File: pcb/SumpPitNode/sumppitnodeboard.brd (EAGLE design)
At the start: 100 x 80 mm, 36 parts, among them IC1 7805T

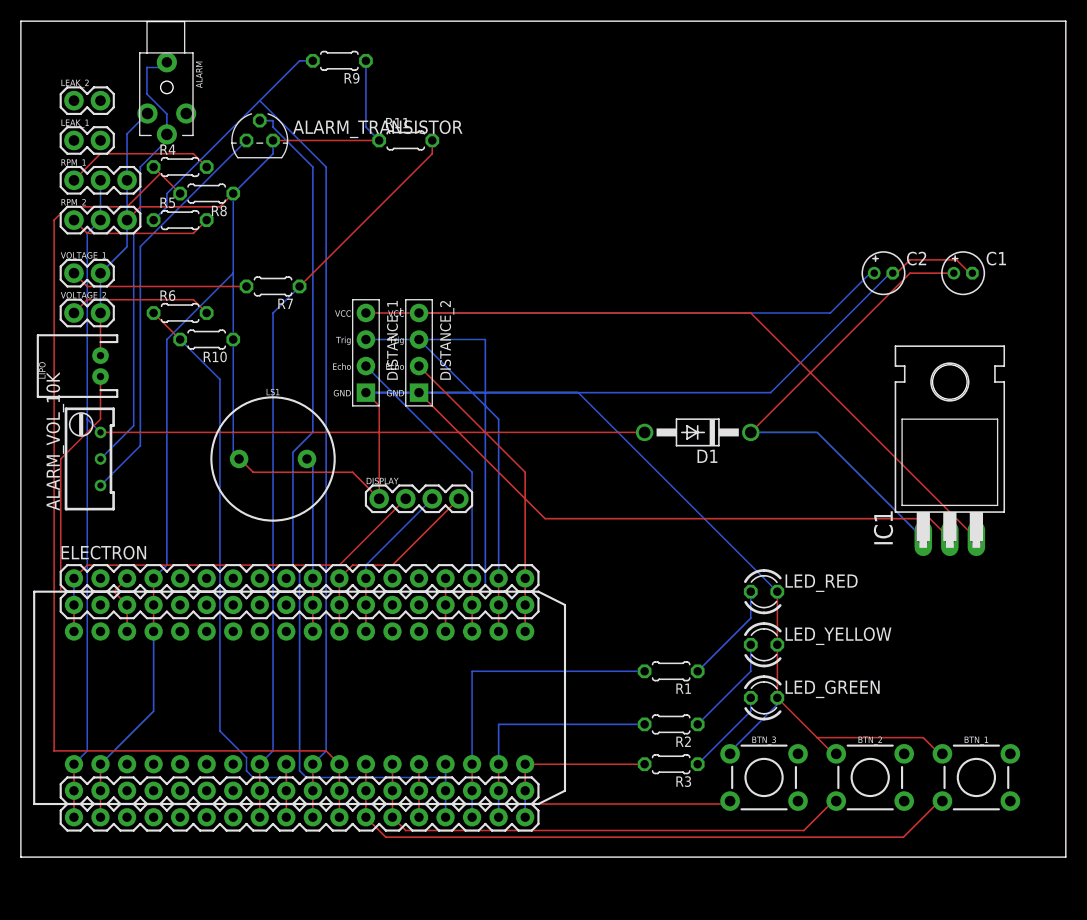
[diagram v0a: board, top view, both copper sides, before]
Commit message: Generate board, connect more sensors.
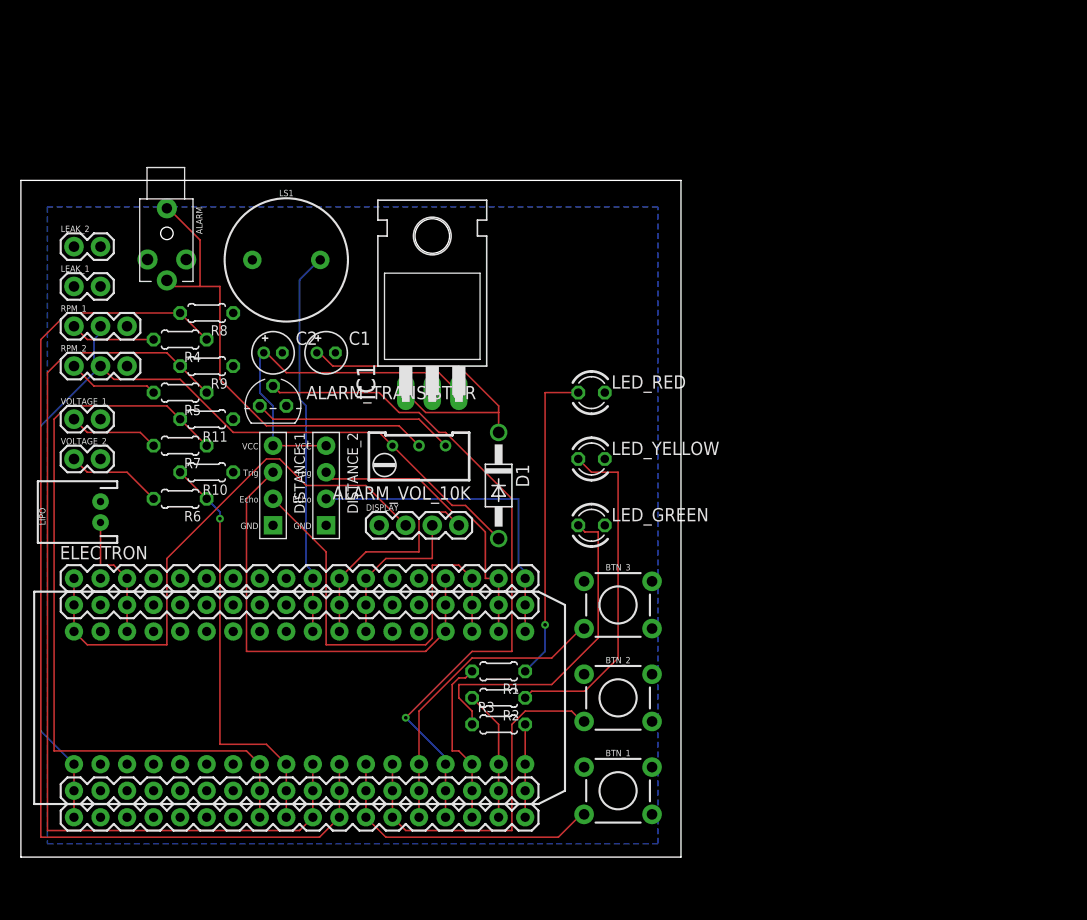
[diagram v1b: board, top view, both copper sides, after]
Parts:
- moved C1 61.4 mm to (29.2, 48.3)
- moved C2 58.9 mm to (24.1, 48.3)
- moved IC1 51.5 mm to (39.4, 54.6)
- moved BTN_1 34.3 mm to (57.1, 6.35)
- moved R11 32.8 mm to (17.8, 41.9), turned to 180 degrees
- moved R9 31.9 mm to (17.8, 47.0)
- moved ALARM_VOL_10K 31.8 mm to (38.1, 38.1), turned to 90 degrees
- moved ALARM_TRANSISTOR 25.4 mm to (24.1, 43.2)
- moved BTN_2 25.3 mm to (57.1, 15.2)
- moved LED_RED 25.2 mm to (54.6, 44.5)
- moved LED_YELLOW 24.3 mm to (54.6, 38.1)
- moved LED_GREEN 23.3 mm to (54.6, 31.8)
- moved BTN_3 21.6 mm to (57.1, 24.1)
- moved D1 19.7 mm to (45.7, 35.6), turned to 270 degrees
- moved LS1 19.1 mm to (25.4, 57.1)
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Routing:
- net GND: track 375.6 -> 0.00 mm
- net N$33: track 112.5 -> 35.1 mm
- net N$10: track 62.4 -> 27.6 mm
- net N$21: track 8.45 -> 31.8 mm
- net N$20: track 9.72 -> 32.6 mm
- net N$8: track 33.4 -> 12.2 mm
- net N$4: track 9.72 -> 30.6 mm, vias 0 -> 1
- net N$22: track 17.1 -> 37.0 mm
- net N$3: track 85.4 -> 65.8 mm, vias 0 -> 1
- net N$2: track 38.8 -> 19.4 mm
- net VCC_1: track 115.9 -> 97.4 mm
- net N$30: track 57.9 -> 39.8 mm, vias 0 -> 1
- net N$18: track 46.5 -> 31.7 mm
- net N$9: track 49.2 -> 35.0 mm
- net N$19: track 30.5 -> 16.3 mm
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- added copper zone on layer 16, net GND
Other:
- board size 100 x 80 mm -> 63.2 x 64.8 mm

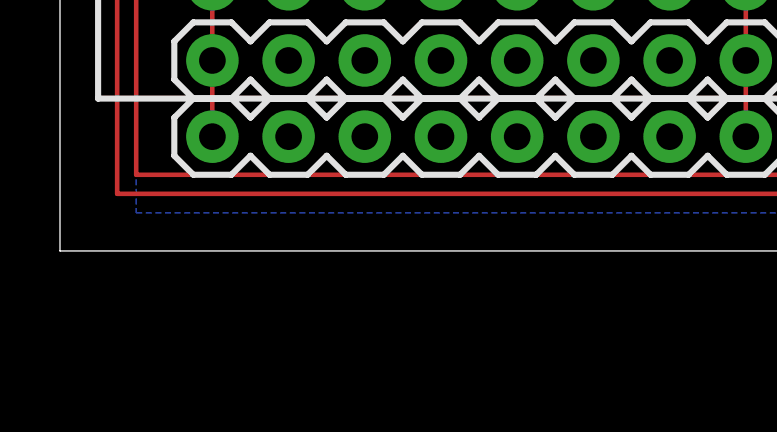
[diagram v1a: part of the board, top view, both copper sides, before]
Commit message: Add relay 4.
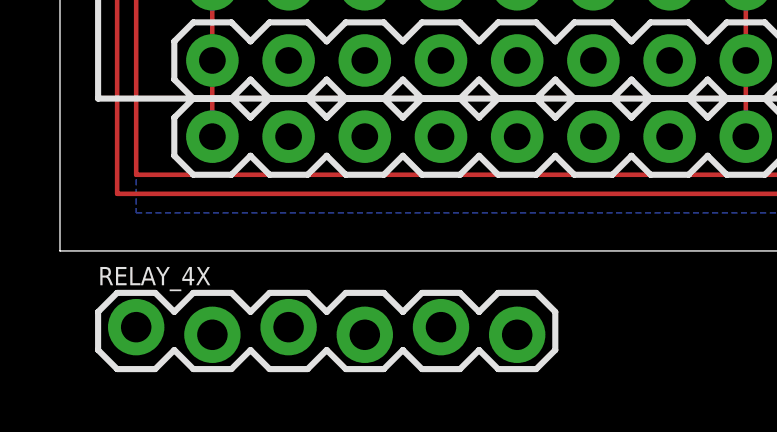
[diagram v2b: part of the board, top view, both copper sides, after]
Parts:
- added RELAY_4X: (no value), SparkFun-Connectors:1X06_LOCK
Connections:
- new net N$34: ELECTRON.63, ELECTRON.99, ELECTRON.D3, RELAY_4X.4
- new net N$35: ELECTRON.62, ELECTRON.98, ELECTRON.D4, RELAY_4X.3
- new net N$36: ELECTRON.61, ELECTRON.97, ELECTRON.D5, RELAY_4X.2
- new net N$37: ELECTRON.60, ELECTRON.96, ELECTRON.D6, RELAY_4X.1
- net GND: now also RELAY_4X.6
- net N$33: now also RELAY_4X.5
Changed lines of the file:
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@@
 <element name="VOLTAGE_2" library="SparkFun-Connectors" library_urn="urn:adsk.eagle:library:513" package="1X02" package3d_urn="urn:adsk.eagle:package:38039/1" value="" x="5.08" y="38.1"/>
 <element name="R11" library="resistor" library_urn="urn:adsk.eagle:library:348" package="0204/5" package3d_urn="urn:adsk.eagle:package:25955/1" value="" x="17.78" y="41.91" rot="R180"/>
+<element name="RELAY_4X" library="SparkFun-Connectors" package="1X06_LOCK" value="" x="2.54" y="-2.54"/>
 </elements>
 <signals>
@@
 <vertex x="60.96" y="62.23"/>
 </polygon>
+<contactref element="RELAY_4X" pad="6"/>
+<wire x1="55.88" y1="38.1" x2="55.88" y2="44.45" width="0" layer="19" extent="1-1"/>
+<wire x1="55.88" y1="31.75" x2="55.88" y2="38.1" width="0" layer="19" extent="1-1"/>
+<wire x1="53.8988" y1="26.3906" x2="55.88" y2="31.75" width="0" layer="19" extent="1-1"/>
+<wire x1="53.8988" y1="17.5006" x2="53.8988" y2="26.3906" width="0" layer="19" extent="1-1"/>
+<wire x1="53.8988" y1="8.6106" x2="53.8988" y2="17.5006" width="0" layer="19" extent="1-1"/>
+<wire x1="39.37" y1="44.45" x2="55.88" y2="44.45" width="0" layer="19" extent="1-1"/>
+<wire x1="30.099" y1="48.26" x2="39.37" y2="44.45" width="0" layer="19" extent="1-1"/>
+<wire x1="25.019" y1="48.26" x2="30.099" y2="48.26" width="0" layer="19" extent="1-1"/>
+<wire x1="20.32" y1="46.99" x2="25.019" y2="48.26" width="0" layer="19" extent="1-1"/>
+<wire x1="20.32" y1="52.07" x2="20.32" y2="46.99" width="0" layer="19" extent="1-1"/>
+<wire x1="25.4" y1="43.18" x2="25.019" y2="48.26" width="0" layer="19" extent="1-1"/>
+<wire x1="20.32" y1="41.91" x2="20.32" y2="46.99" width="0" layer="19" extent="1-1"/>
+<wire x1="20.32" y1="36.83" x2="20.32" y2="41.91" width="0" layer="19" extent="1-1"/>
+<wire x1="22.15" y1="57.15" x2="20.32" y2="52.07" width="0" layer="19" extent="1-1"/>
+<wire x1="24.13" y1="31.75" x2="20.32" y2="36.83" width="0" layer="19" extent="1-1"/>
+<wire x1="29.21" y1="31.75" x2="24.13" y2="31.75" width="0" layer="19" extent="1-1"/>
+<wire x1="34.29" y1="31.75" x2="29.21" y2="31.75" width="0" layer="19" extent="1-1"/>
+<wire x1="12.12" y1="57.19" x2="20.32" y2="52.07" width="0" layer="19" extent="1-1"/>
+<wire x1="10.16" y1="50.8" x2="12.12" y2="57.19" width="0" layer="19" extent="1-1"/>
+<wire x1="10.16" y1="46.99" x2="10.16" y2="50.8" width="0" layer="19" extent="1-1"/>
+<wire x1="7.62" y1="41.91" x2="10.16" y2="46.99" width="0" layer="19" extent="1-1"/>
+<wire x1="7.62" y1="38.1" x2="7.62" y2="41.91" width="0" layer="19" extent="1-1"/>
+<wire x1="7.62" y1="34.02" x2="7.62" y2="38.1" width="0" layer="19" extent="1-1"/>
+<wire x1="12.7" y1="26.67" x2="7.62" y2="34.02" width="0" layer="19" extent="1-1"/>
+<wire x1="12.7" y1="24.13" x2="12.7" y2="26.67" width="0" layer="19" extent="1-1"/>
+<wire x1="12.7" y1="21.59" x2="12.7" y2="24.13" width="0" layer="19" extent="1-1"/>
+<wire x1="7.62" y1="8.89" x2="12.7" y2="21.59" width="0" layer="19" extent="1-1"/>
+<wire x1="7.62" y1="6.35" x2="7.62" y2="8.89" width="0" layer="19" extent="1-1"/>
+<wire x1="7.62" y1="3.81" x2="7.62" y2="6.35" width="0" layer="19" extent="1-1"/>
+<wire x1="15.24" y1="-2.794" x2="7.62" y2="3.81" width="0" layer="19" extent="1-1"/>
 </signal>
 <signal name="N$1">
@@
 <wire x1="22.86" y1="48.26" x2="22.86" y2="44.45" width="0.1524" layer="16"/>
 <wire x1="22.86" y1="48.26" x2="23.241" y2="48.26" width="0.1524" layer="16"/>
+<contactref element="RELAY_4X" pad="5"/>
+<wire x1="12.7" y1="-2.54" x2="24.13" y2="39.37" width="0" layer="19" extent="1-1"/>
+</signal>
+<signal name="N$34">
+<contactref element="RELAY_4X" pad="4"/>
+<contactref element="ELECTRON" pad="63"/>
+<contactref element="ELECTRON" pad="99"/>
+<contactref element="ELECTRON" pad="D3"/>
+<wire x1="25.4" y1="24.13" x2="25.4" y2="26.67" width="0" layer="19" extent="1-1"/>
+<wire x1="25.4" y1="21.59" x2="25.4" y2="24.13" width="0" layer="19" extent="1-1"/>
+<wire x1="10.16" y1="-2.794" x2="25.4" y2="21.59" width="0" layer="19" extent="1-1"/>
+</signal>
+<signal name="N$35">
+<contactref element="RELAY_4X" pad="3"/>
+<contactref element="ELECTRON" pad="98"/>
+<contactref element="ELECTRON" pad="62"/>
+<contactref element="ELECTRON" pad="D4"/>
+<wire x1="22.86" y1="24.13" x2="22.86" y2="26.67" width="0" layer="19" extent="1-1"/>
+<wire x1="22.86" y1="21.59" x2="22.86" y2="24.13" width="0" layer="19" extent="1-1"/>
+<wire x1="7.62" y1="-2.54" x2="22.86" y2="21.59" width="0" layer="19" extent="1-1"/>
+</signal>
+<signal name="N$36">
+<contactref element="RELAY_4X" pad="2"/>
+<contactref element="ELECTRON" pad="97"/>
+<contactref element="ELECTRON" pad="D5"/>
+<contactref element="ELECTRON" pad="61"/>
+<wire x1="20.32" y1="24.13" x2="20.32" y2="26.67" width="0" layer="19" extent="1-1"/>
+<wire x1="20.32" y1="21.59" x2="20.32" y2="24.13" width="0" layer="19" extent="1-1"/>
+<wire x1="5.08" y1="-2.794" x2="20.32" y2="21.59" width="0" layer="19" extent="1-1"/>
+</signal>
+<signal name="N$37">
+<contactref element="RELAY_4X" pad="1"/>
+<contactref element="ELECTRON" pad="D6"/>
+<contactref element="ELECTRON" pad="60"/>
+<contactref element="ELECTRON" pad="96"/>
+<wire x1="17.78" y1="24.13" x2="17.78" y2="26.67" width="0" layer="19" extent="1-1"/>
+<wire x1="17.78" y1="21.59" x2="17.78" y2="24.13" width="0" layer="19" extent="1-1"/>
+<wire x1="2.54" y1="-2.54" x2="17.78" y2="21.59" width="0" layer="19" extent="1-1"/>
 </signal>
 </signals>
